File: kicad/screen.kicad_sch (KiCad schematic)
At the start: 1 part, among them J7 DO0180FMST03

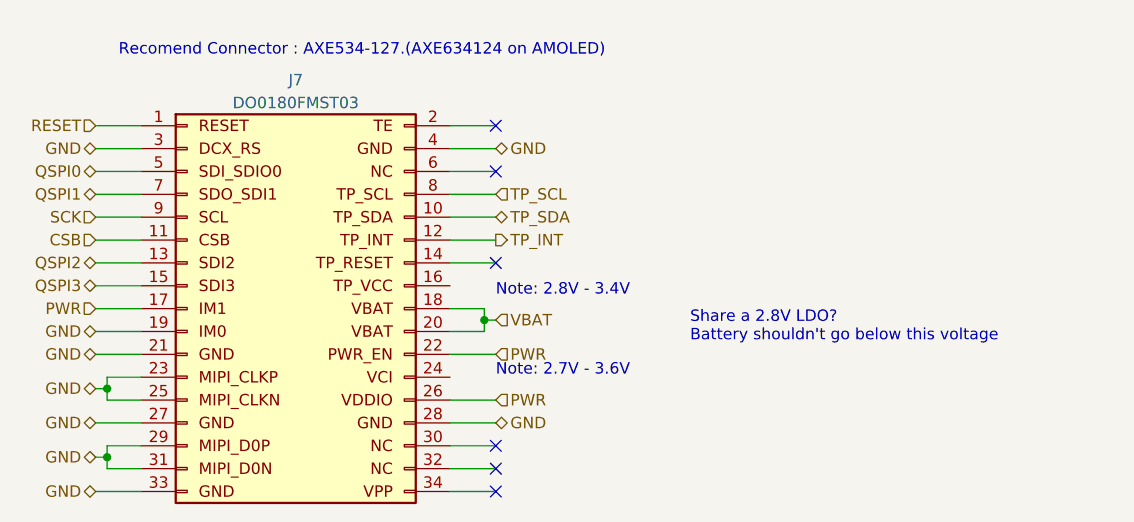
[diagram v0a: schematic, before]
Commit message: Update schematic and add basic PCB layout
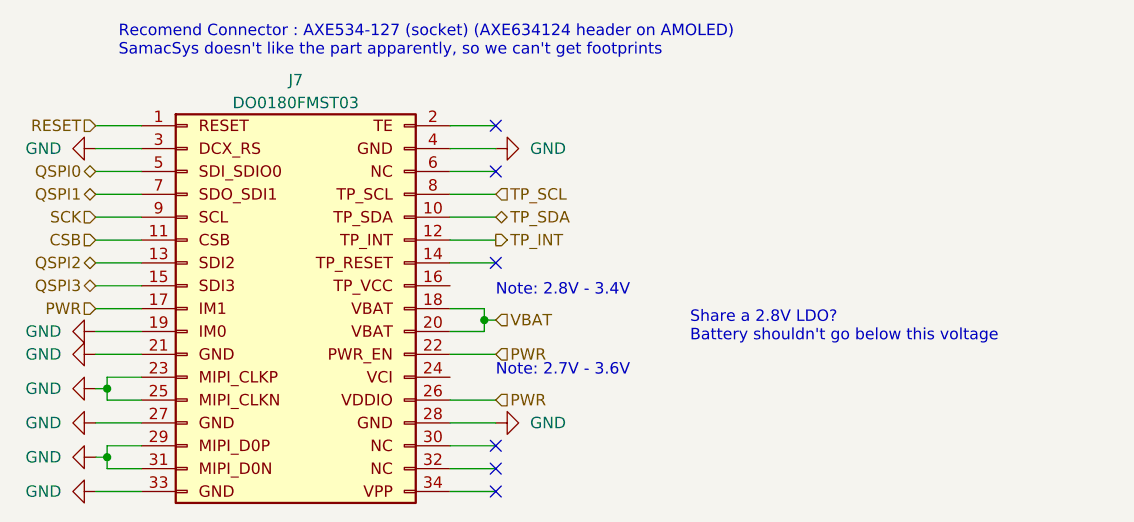
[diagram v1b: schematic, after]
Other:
- note added: "Recomend Connector : AXE534-127 (socket) (AXE634124 header on AMOLED) SamacSys doesn't like the part apparently, so we can't get footprints"
- note removed: "Recomend Connector : AXE534-127.(AXE634124 on AMOLED)"

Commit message: hw: update power symbols, clean up some power circuitry
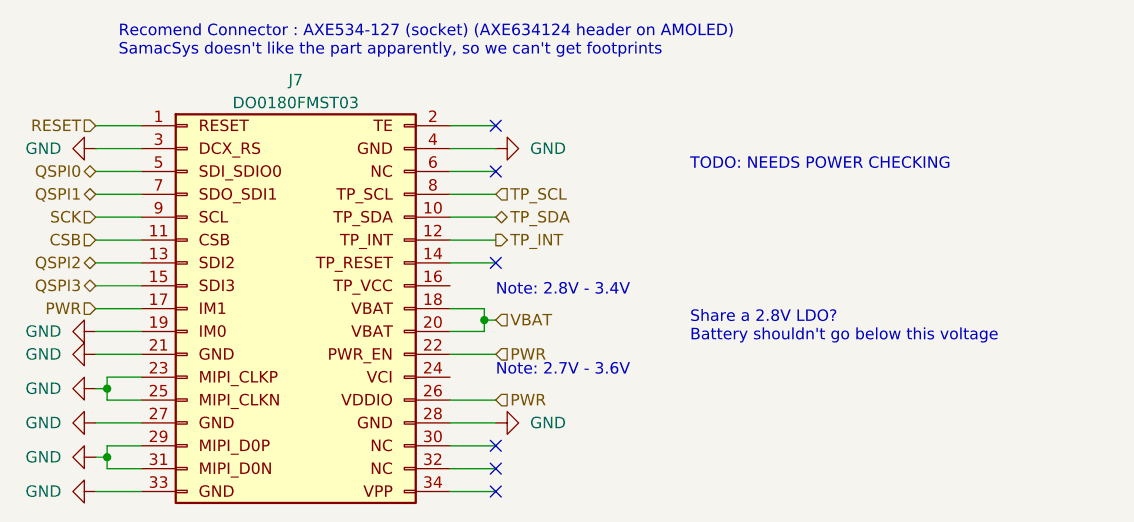
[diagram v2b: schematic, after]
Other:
- note added: "TODO: NEEDS POWER CHECKING"
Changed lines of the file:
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@@
+    (effects (font (size 1.27 1.27)) (justify left bottom))
+  )
+  (text "TODO: NEEDS POWER CHECKING" (at 224.79 58.42 0)
     (effects (font (size 1.27 1.27)) (justify left bottom))
   )
